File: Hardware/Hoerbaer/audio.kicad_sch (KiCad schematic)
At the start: 38 parts, among them J14 Speaker_L, J15 Speaker_R, U10 TAS5805M

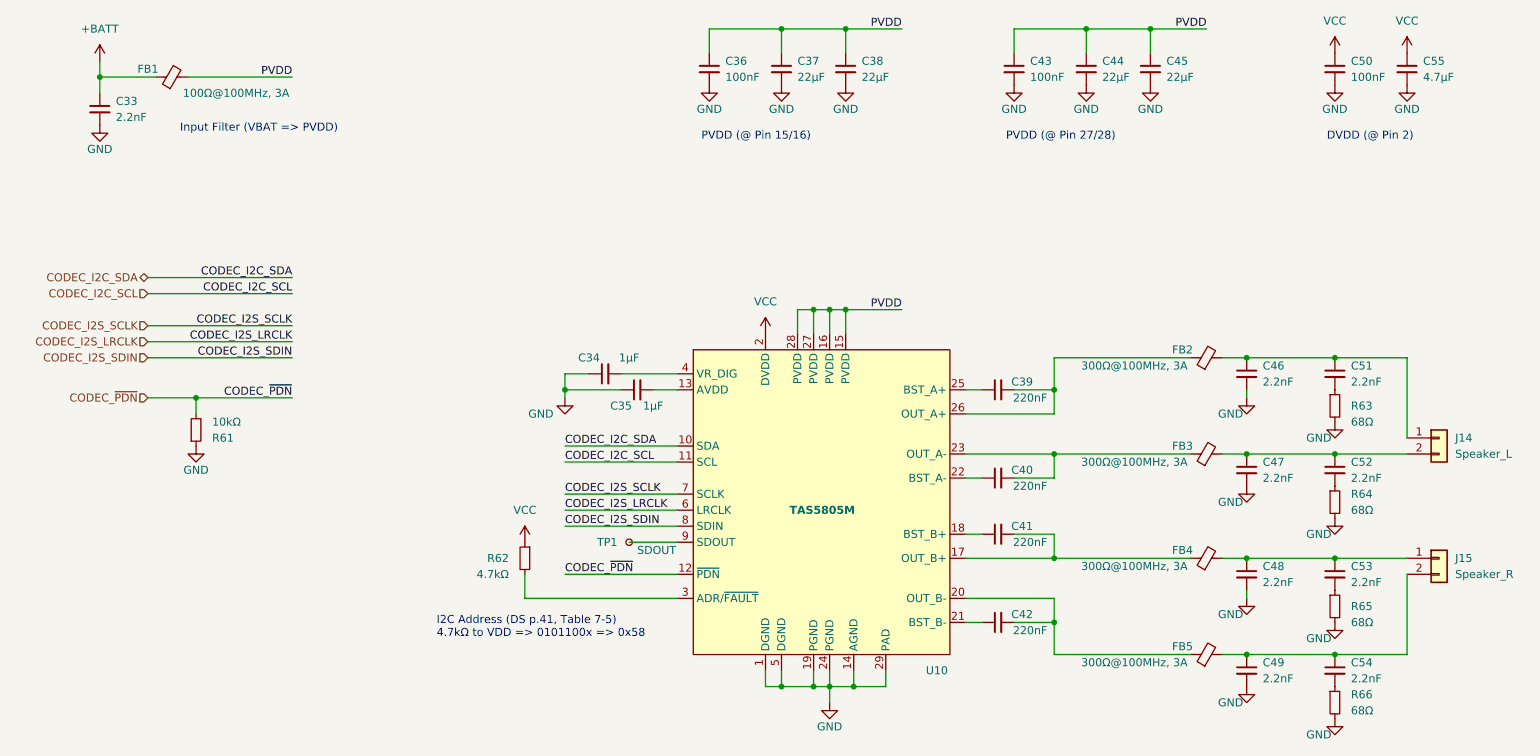
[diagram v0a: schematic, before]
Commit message: Nearly complete schematic with TLV61048 as 12V booster.
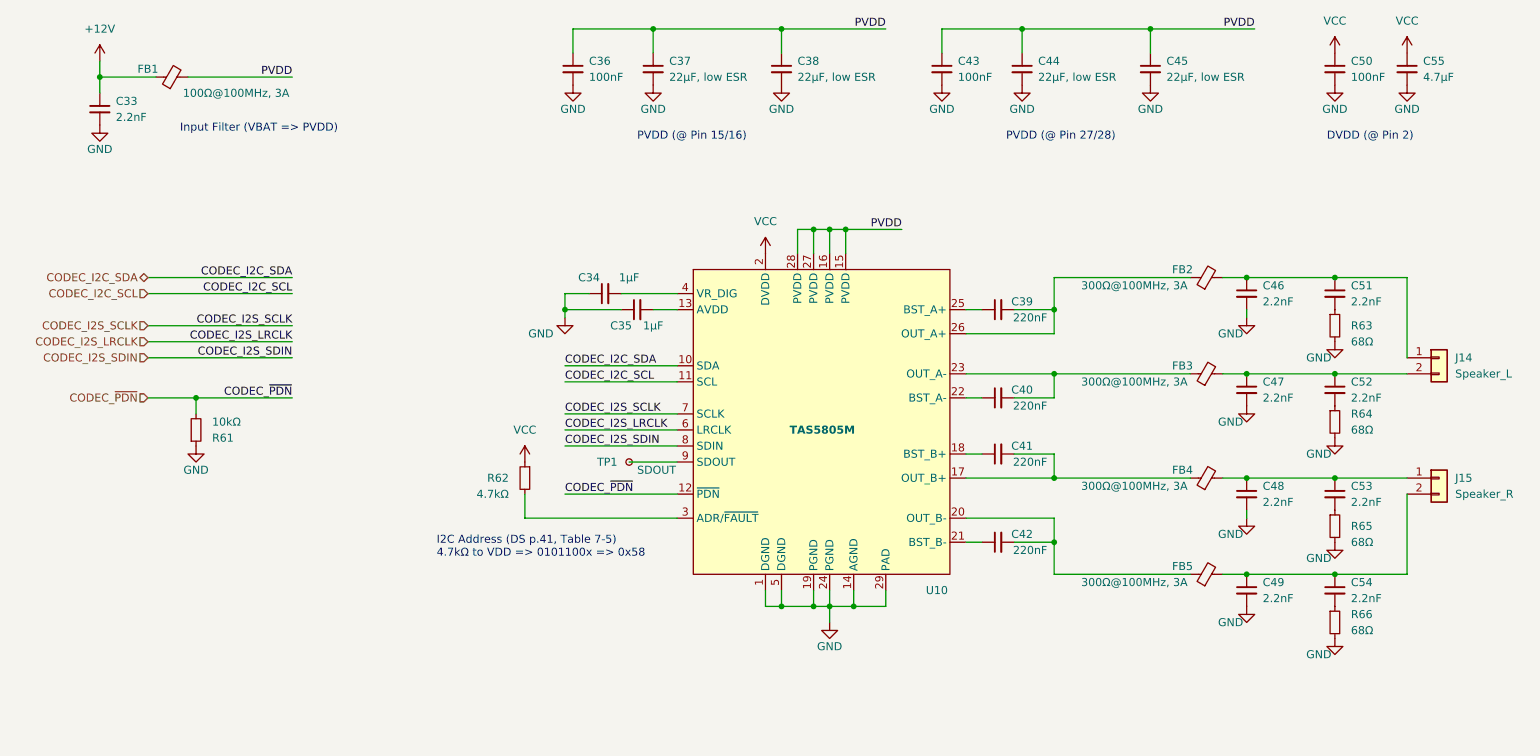
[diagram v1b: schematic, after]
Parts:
- C37, C38, C44, C45: value 22µF -> 22µF, low ESR
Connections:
- net +BATT renamed +12V
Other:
- company: (none) -> Drachosaurus Designs
- title: (none) -> Hör Bär main
- moved on the sheet: C34, C35, C36, C37, C38, C39, C40, C41, C42, C43, C44, C46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

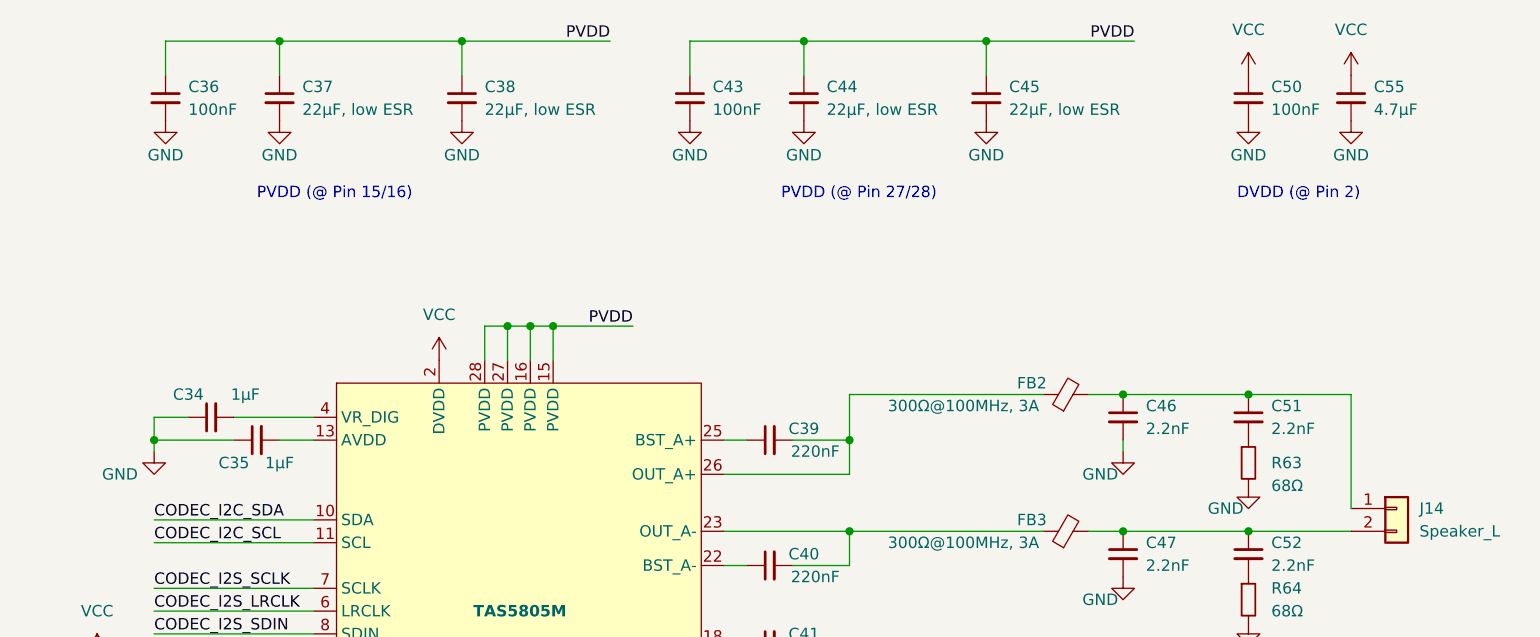
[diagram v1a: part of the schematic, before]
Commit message: Footprints, order numbers, ...
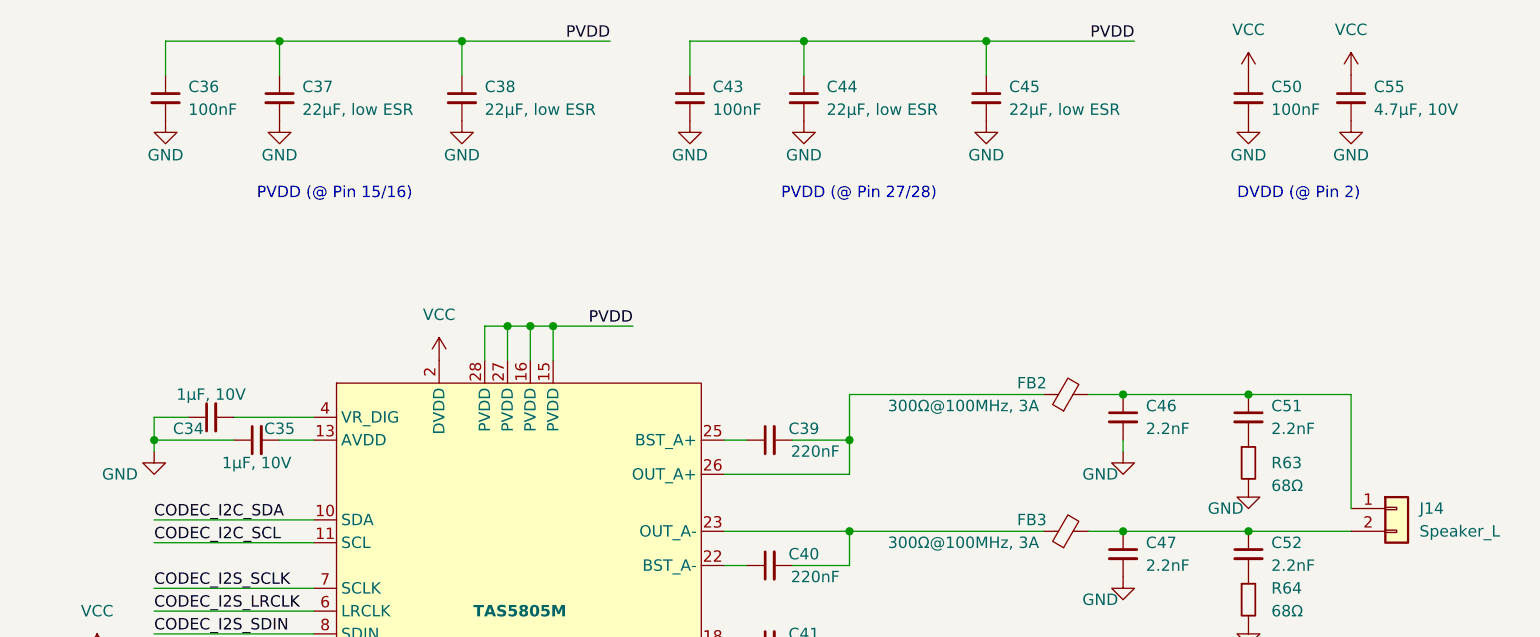
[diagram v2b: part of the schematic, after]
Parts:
- C33, C36, C39, C40, C41, C42, C43, C46, C47, C48, C49, C50, C51, C52, C53, C54: footprint (none) -> Capacitor_SMD:C_0402_1005Metric
- C34, C35: value 1µF -> 1µF, 10V; footprint (none) -> Capacitor_SMD:C_0402_1005Metric; JLCPCB (none) -> C726581; MPN (none) -> AC0805KKX7R6BB105
- C37, C38, C44, C45: footprint (none) -> Capacitor_SMD:C_1210_3225Metric; JLCPCB (none) -> C6120032; MPN (none) -> CGA1210X7R226K250RT
- C55: value 4.7µF -> 4.7µF, 10V; footprint (none) -> Capacitor_SMD:C_0805_2012Metric; JLCPCB (none) -> C361188; MPN (none) -> C2012X7R1A475KT0J0E
- R61, R62, R63, R64, R65, R66: footprint (none) -> Resistor_SMD:R_0402_1005Metric
- TP1: footprint (none) -> TestPoint:TestPoint_Pad_D1.5mm

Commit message: More numbers, changed HBI input package, i2c addresses, layout.
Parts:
- J14, J15: footprint Connector_Wire:SolderWire-0.75sqmm_1x02_P7mm_D1.25mm_OD3.5mm -> Connector_Phoenix_MSTB:PhoenixContact_MSTBVA_2,5_2-G-5,08_1x02_P5.08mm_Vertical
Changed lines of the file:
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@@
       (effects (font (size 1.27 1.27)) (justify left))
     )
-    (property "Footprint" "Connector_Wire:SolderWire-0.75sqmm_1x02_P7mm_D1.25mm_OD3.5mm" (at 245.11 85.09 0)
+    (property "Footprint" "Connector_Phoenix_MSTB:PhoenixContact_MSTBVA_2,5_2-G-5,08_1x02_P5.08mm_Vertical" (at 245.11 85.09 0)
       (effects (font (size 1.27 1.27)) hide)
     )
@@
       (effects (font (size 1.27 1.27)) (justify left))
     )
-    (property "Footprint" "Connector_Wire:SolderWire-0.75sqmm_1x02_P7mm_D1.25mm_OD3.5mm" (at 245.11 104.14 0)
-      (effects (font (size 1.27 1.27)) hide)
-    )
+    (property "Footprint" "Connector_Phoenix_MSTB:PhoenixContact_MSTBVA_2,5_2-G-5,08_1x02_P5.08mm_Vertical" (at 245.11 104.14 0)
+      (effects (font (size 1.27 1.27)) hide)
+    )

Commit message: Layout drc error free
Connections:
- net SPEAKER_B-: now reaches C49.1, C54.1, FB5.2, J15.2 (Pin_2)
- net SPEAKER_A-: now reaches C47.1, C52.1, FB3.2, J14.2 (Pin_2)
- net AMP_OUT_B+: now reaches C41.2, FB4.1, U10.17 (OUT_B+)
- net SPEAKER_A+: now reaches C46.1, C51.1, FB2.2, J14.1 (Pin_1)
- net SPEAKER_B+: now reaches C48.1, C53.1, FB4.2, J15.1 (Pin_1)
- net AMP_OUT_B-: now reaches C42.2, FB5.1, U10.20 (OUT_B-)
- net AMP_OUT_A+: now reaches C39.2, FB2.1, U10.26 (OUT_A+)
- net AMP_OUT_A-: now reaches C40.2, FB3.1, U10.23 (OUT_A-)
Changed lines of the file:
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@@
     (effects (font (size 1.27 1.27)) (justify right bottom))
   )
+  (label "AMP_OUT_A-" (at 184.15 87.63 0) (fields_autoplaced)
+    (effects (font (size 1.27 1.27)) (justify left bottom))
+  )
+  (label "AMP_OUT_A+" (at 184.15 72.39 0) (fields_autoplaced)
+    (effects (font (size 1.27 1.27)) (justify left bottom))
+  )
   (label "CODEC_I2C_SCL" (at 106.68 88.9 0) (fields_autoplaced)
+    (effects (font (size 1.27 1.27)) (justify left bottom))
+  )
+  (label "SPEAKER_B-" (at 214.63 119.38 0) (fields_autoplaced)
+    (effects (font (size 1.27 1.27)) (justify left bottom))
+  )
+  (label "AMP_OUT_B-" (at 184.15 114.3 0) (fields_autoplaced)
+    (effects (font (size 1.27 1.27)) (justify left bottom))
+  )
+  (label "SPEAKER_A-" (at 214.63 87.63 0) (fields_autoplaced)
     (effects (font (size 1.27 1.27)) (justify left bottom))
   )
@@
     (effects (font (size 1.27 1.27)) (justify right bottom))
   )
+  (label "AMP_OUT_B+" (at 184.15 104.14 0) (fields_autoplaced)
+    (effects (font (size 1.27 1.27)) (justify left bottom))
+  )
+  (label "SPEAKER_A+" (at 214.63 72.39 0) (fields_autoplaced)
+    (effects (font (size 1.27 1.27)) (justify left bottom))
+  )
+  (label "SPEAKER_B+" (at 214.63 104.14 0) (fields_autoplaced)
+    (effects (font (size 1.27 1.27)) (justify left bottom))
+  )
   (label "CODEC_I2S_SCLK" (at 106.68 93.98 0) (fields_autoplaced)
     (effects (font (size 1.27 1.27)) (justify left bottom))
@@
     (effects (font (size 1.27 1.27)) (justify right))
   )
+  (netclass_flag "" (length 2.54) (shape round) (at 184.15 110.49 0) (fields_autoplaced)
+    (effects (font (size 1.27 1.27)) (justify left bottom))
+    (property "Netclass" "SPEAKER" (at 184.8485 107.95 0)
+      (effects (font (size 1.27 1.27) italic) (justify left))
+    )
+  )
+  (netclass_flag "" (length 2.54) (shape round) (at 240.03 72.39 0) (fields_autoplaced)
+    (effects (font (size 1.27 1.27)) (justify left bottom))
+    (property "Netclass" "SPEAKER" (at 240.7285 69.85 0)
+      (effects (font (size 1.27 1.27) italic) (justify left))
+    )
+  )
+  (netclass_flag "" (length 2.54) (shape round) (at 171.45 114.3 180) (fields_autoplaced)
+    (effects (font (size 1.27 1.27)) (justify right bottom))
+    (property "Netclass" "SPEAKER" (at 172.1485 116.84 0)
+      (effects (font (size 1.27 1.27) italic) (justify left))
+    )
+  )
+  (netclass_flag "" (length 2.54) (shape round) (at 184.15 100.33 0) (fields_autoplaced)
+    (effects (font (size 1.27 1.27)) (justify left bottom))
+    (property "Netclass" "SPEAKER" (at 184.8485 97.79 0)
+      (effects (font (size 1.27 1.27) italic) (justify left))
+    )
+  )
+  (netclass_flag "" (length 2.54) (shape round) (at 184.15 72.39 0)
+    (effects (font (size 1.27 1.27)) (justify left bottom))
+    (property "Netclass" "SPEAKER" (at 184.15 68.58 0)
+      (effects (font (size 1.27 1.27) italic) (justify left))
+    )
+  )
+  (netclass_flag "" (length 2.54) (shape round) (at 171.45 91.44 180) (fields_autoplaced)
+    (effects (font (size 1.27 1.27)) (justify right bottom))
+    (property "Netclass" "SPEAKER" (at 172.1485 93.98 0)
+      (effects (font (size 1.27 1.27) italic) (justify left))
+    )
+  )
+  (netclass_flag "" (length 2.54) (shape round) (at 171.45 77.47 0) (fields_autoplaced)
+    (effects (font (size 1.27 1.27)) (justify left bottom))
+    (property "Netclass" "SPEAKER" (at 172.1485 74.93 0)
+      (effects (font (size 1.27 1.27) italic) (justify left))
+    )
+  )
+  (netclass_flag "" (length 2.54) (shape round) (at 184.15 87.63 0)
+    (effects (font (size 1.27 1.27)) (justify left bottom))
+    (property "Netclass" "SPEAKER" (at 184.15 83.82 0)
+      (effects (font (size 1.27 1.27) italic) (justify left))
+    )
+  )
+  (netclass_flag "" (length 2.54) (shape round) (at 240.03 119.38 180) (fields_autoplaced)
+    (effects (font (size 1.27 1.27)) (justify right bottom))
+    (property "Netclass" "SPEAKER" (at 240.7285 121.92 0)
+      (effects (font (size 1.27 1.27) italic) (justify left))
+    )
+  )
+  (netclass_flag "" (length 2.54) (shape round) (at 171.45 100.33 0) (fields_autoplaced)
+    (effects (font (size 1.27 1.27)) (justify left bottom))
+    (property "Netclass" "SPEAKER" (at 172.1485 97.79 0)
+      (effects (font (size 1.27 1.27) italic) (justify left))
+    )
+  )
+  (netclass_flag "" (length 2.54) (shape round) (at 240.03 87.63 180) (fields_autoplaced)
+    (effects (font (size 1.27 1.27)) (justify right bottom))
+    (property "Netclass" "SPEAKER" (at 240.7285 90.17 0)
+      (effects (font (size 1.27 1.27) italic) (justify left))
+    )
+  )
+  (netclass_flag "" (length 2.54) (shape round) (at 240.03 104.14 0) (fields_autoplaced)
+    (effects (font (size 1.27 1.27)) (justify left bottom))
+    (property "Netclass" "SPEAKER" (at 240.7285 101.6 0)
+      (effects (font (size 1.27 1.27) italic) (justify left))
+    )
+  )
   (symbol (lib_id "Device:C_Small") (at 113.03 74.93 90) (unit 1)
     (in_bom yes) (on_board yes) (dnp no)
@@
       (effects (font (size 1.27 1.27)) hide)
     )
-    (property "Value" "GND" (at 226.06 132.08 0)
+    (property "Value" "GND" (at 231.14 132.08 0)
       (effects (font (size 1.27 1.27)))
     )
@@
       (effects (font (size 1.27 1.27)) hide)
     )
-    (property "Value" "GND" (at 226.06 100.33 0)
+    (property "Value" "GND" (at 231.14 100.33 0)
       (effects (font (size 1.27 1.27)))
     )
@@
       (effects (font (size 1.27 1.27)) hide)
     )
-    (property "Value" "GND" (at 226.06 85.09 0)
+    (property "Value" "GND" (at 231.14 85.09 0)
       (effects (font (size 1.27 1.27)))
     )
@@
       (effects (font (size 1.27 1.27)) hide)
     )
-    (property "Value" "GND" (at 226.06 116.84 0)
-      (effects (font (size 1.27 1.27)))
-    )
+    (property "Value" "GND" (at 231.14 116.84 0)
+      (effects (font (size 1.27 1.27)))
+    )

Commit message: Drachosaurus added
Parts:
- removed TP1: SDOUT, TestPoint:TestPoint_Pad_D1.5mm, symbol Connector:TestPoint_Small
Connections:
- no-connect marks 0 -> 1
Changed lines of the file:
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@@
   (junction (at 106.68 77.47) (diameter 0) (color 0 0 0 0)
   )
+  (no_connect (at 124.46 101.6))
   (wire (pts (xy 152.4 121.92) (xy 152.4 124.46))
     (stroke (width 0) (type default))
@@
     (stroke (width 0) (type default))
   )
-  (wire (pts (xy 116.84 101.6) (xy 124.46 101.6))
-    (stroke (width 0) (type default))
-  )
   (wire (pts (xy 40.64 91.44) (xy 48.26 91.44))
     (stroke (width 0) (type default))
@@
         )
       )
-    )
-  )
-  (symbol (lib_id "Connector:TestPoint_Small") (at 116.84 101.6 0) (unit 1)
-    (in_bom yes) (on_board yes) (dnp no)
-    (property "Reference" "TP1" (at 111.76 101.6 0)
-      (effects (font (size 1.27 1.27)) (justify left))
-    )
-    (property "Value" "SDOUT" (at 118.11 102.87 0)
-      (effects (font (size 1.27 1.27)) (justify left))
-    )
-    (property "Footprint" "TestPoint:TestPoint_Pad_D1.5mm" (at 121.92 101.6 0)
-      (effects (font (size 1.27 1.27)) hide)
-    )
-    (property "Datasheet" "~" (at 121.92 101.6 0)
-      (effects (font (size 1.27 1.27)) hide)
-    )
-    (pin "1")
-    (instances
-      (project "Hoerbaer"
-        (path "/31f16f54-0469-45ae-b442-d363bf5fad3b/9dcf3cb0-d097-46a7-98e7-f495dabb37d0"
-          (reference "TP1") (unit 1)
-        )
-      )
